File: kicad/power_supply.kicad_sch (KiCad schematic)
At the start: 47 parts, among them J2 Conn_01x02_Female, Q1 2N2905A, Q2 2N2905A, Q3 BC148, Q4 BC148, T1 Transformer_1P_2S, U11 7406, U18 LM7805_TO220, U19 LM317SP_TO220, U20 LM317L_TO92

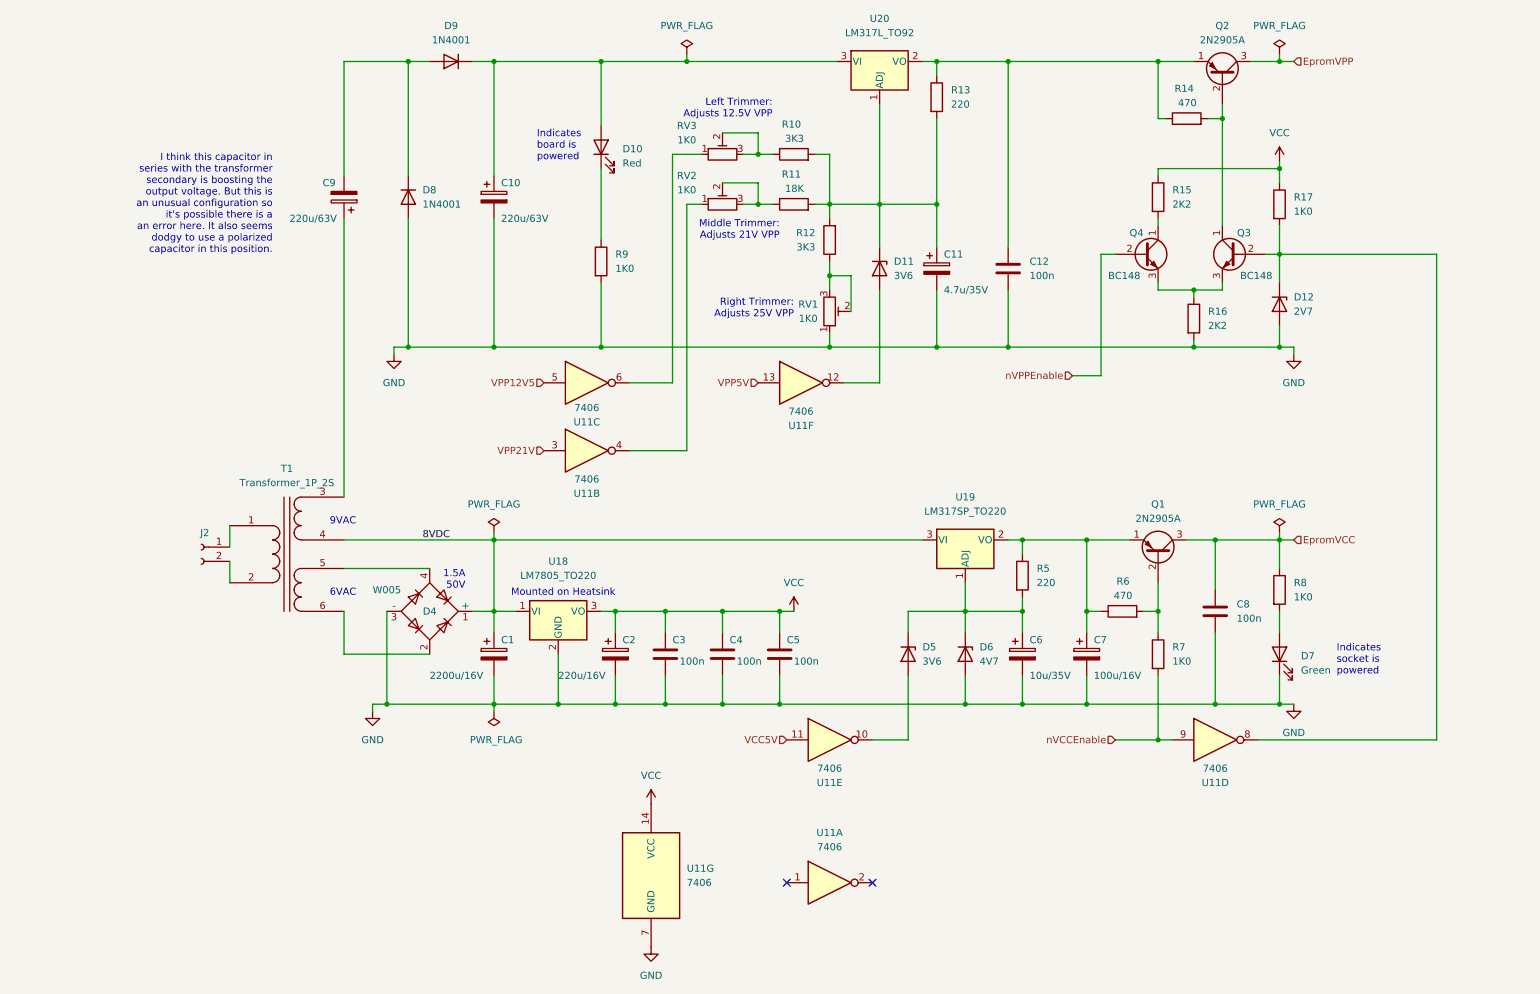
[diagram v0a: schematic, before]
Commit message: Fixed following stardot discussion of PSU, and review of issue 2 photos
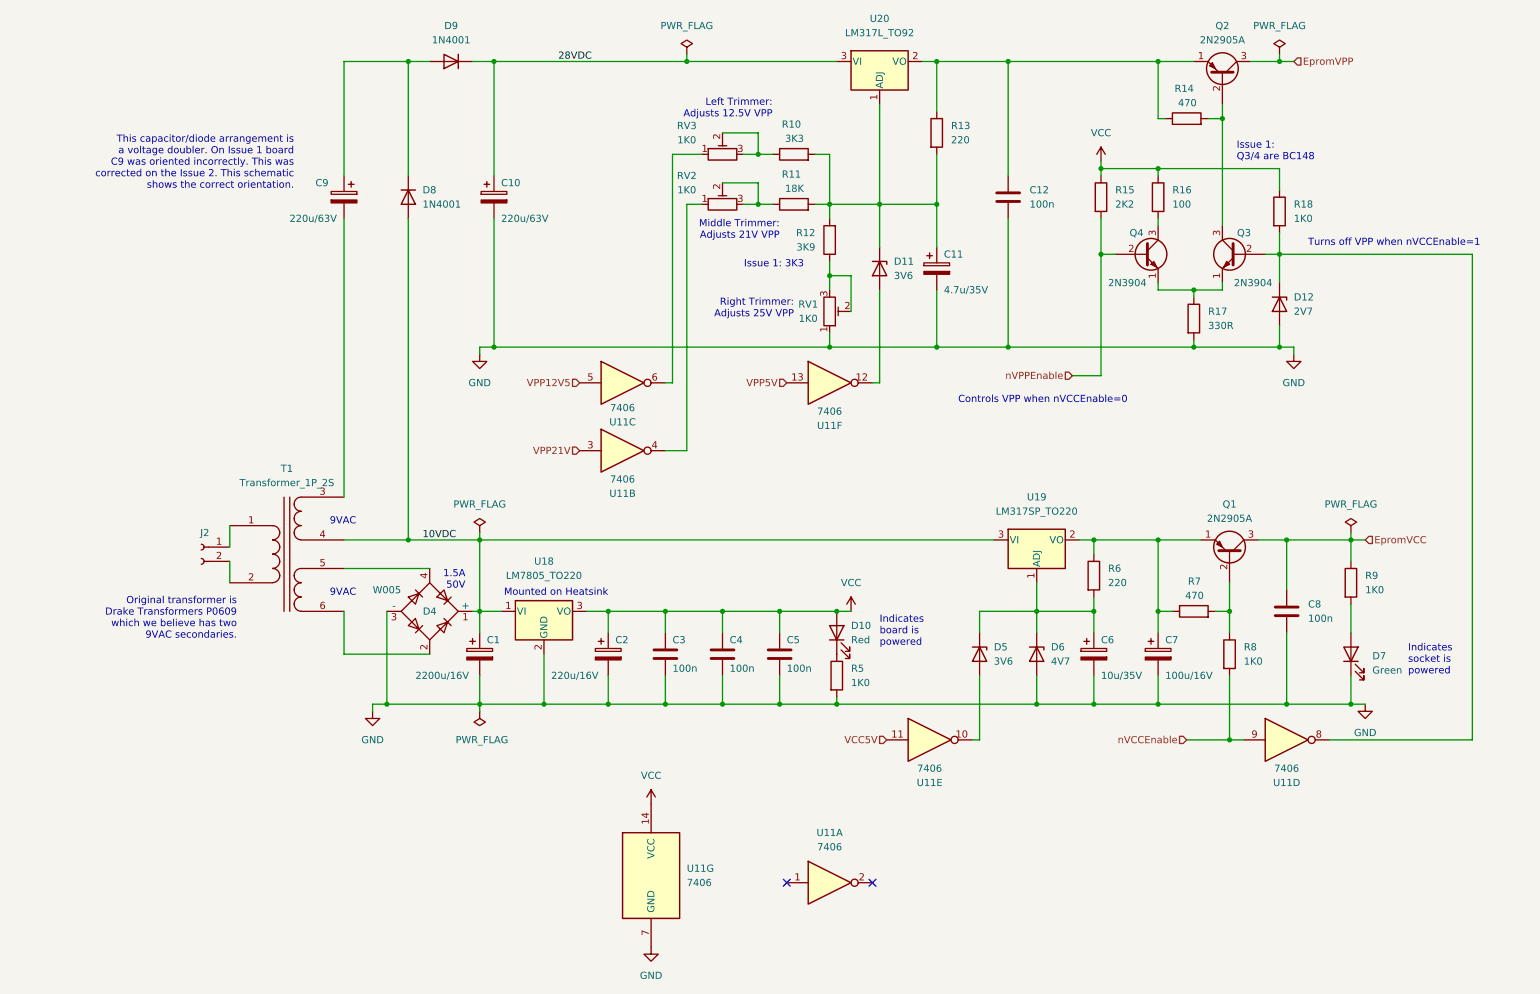
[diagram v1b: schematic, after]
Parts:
- removed Q3, Q4: BC148, Package_TO_SOT_THT:TO-92_Inline, symbol Transistor_BJT:BC548
- added Q3, Q4: 2N3904, Package_TO_SOT_THT:TO-92_Inline, symbol Transistor_BJT:2N3904
- added R16: 100, symbol Device:R
- R12: value 3K3 -> 3K9
- R17: renamed from R16; value 2K2 -> 330R
- renumbered R17 to R18, R9 to R5, R5 to R6, R6 to R7, R7 to R8, R8 to R9
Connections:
- net GND: no longer D8.2 (A)
- net VCC: now also D10.2 (A), R16.1
- net nVPPEnable: now also R15.2, Q4.2 (B)
- net at Q2.2 (B), R14.2: now also Q3.3 (C)
- net at D12.1 (K), R18.2, U11.8: now also Q3.2 (B)
- net at R17.1: now also Q3.1 (E), Q4.1 (E)
- net at T1.3 (SA): now also C9.2; no longer C9.1
- net at D8.1 (K), D9.2 (A): now also C9.1; no longer C9.2
- net 28VDC: now reaches C10.1, D9.1 (K), U20.3 (VI)
- net 28VDC: no longer D10.2 (A)
- net 8VDC renamed 10VDC
- net 10VDC: now also D8.2 (A)
- new net: Q4.3 (C), R16.2
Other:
- note added: "Controls VPP when nVCCEnable=0"
- note added: "Issue 1: 3K3"
- note added: "Issue 1: Q3/4 are BC148"
- note added: "Original transformer is Drake Transformers P0609 which we believe has two 9VAC secondaries."
- note added: "This capacitor/diode arrangement is a voltage doubler. On Issue 1 board C9 was oriented incorrectly. This was corrected on the Issue 2. This schematic shows the correct orientation."
- note added: "Turns off VPP when nVCCEnable=1"
- note removed: "6VAC"
- note removed: "I think this capacitor in series with the transformer secondary is boosting the output voltage. But this is an unusual configuration so it's possible there is a an error here. It also seems dodgy to use a polarized capacitor in this position."
- moved on the sheet: C1, C12, C2, C6, C7, C8, C9, D10, D5, D6, D7, Q1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

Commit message: KiCAD: Initial PCB placement
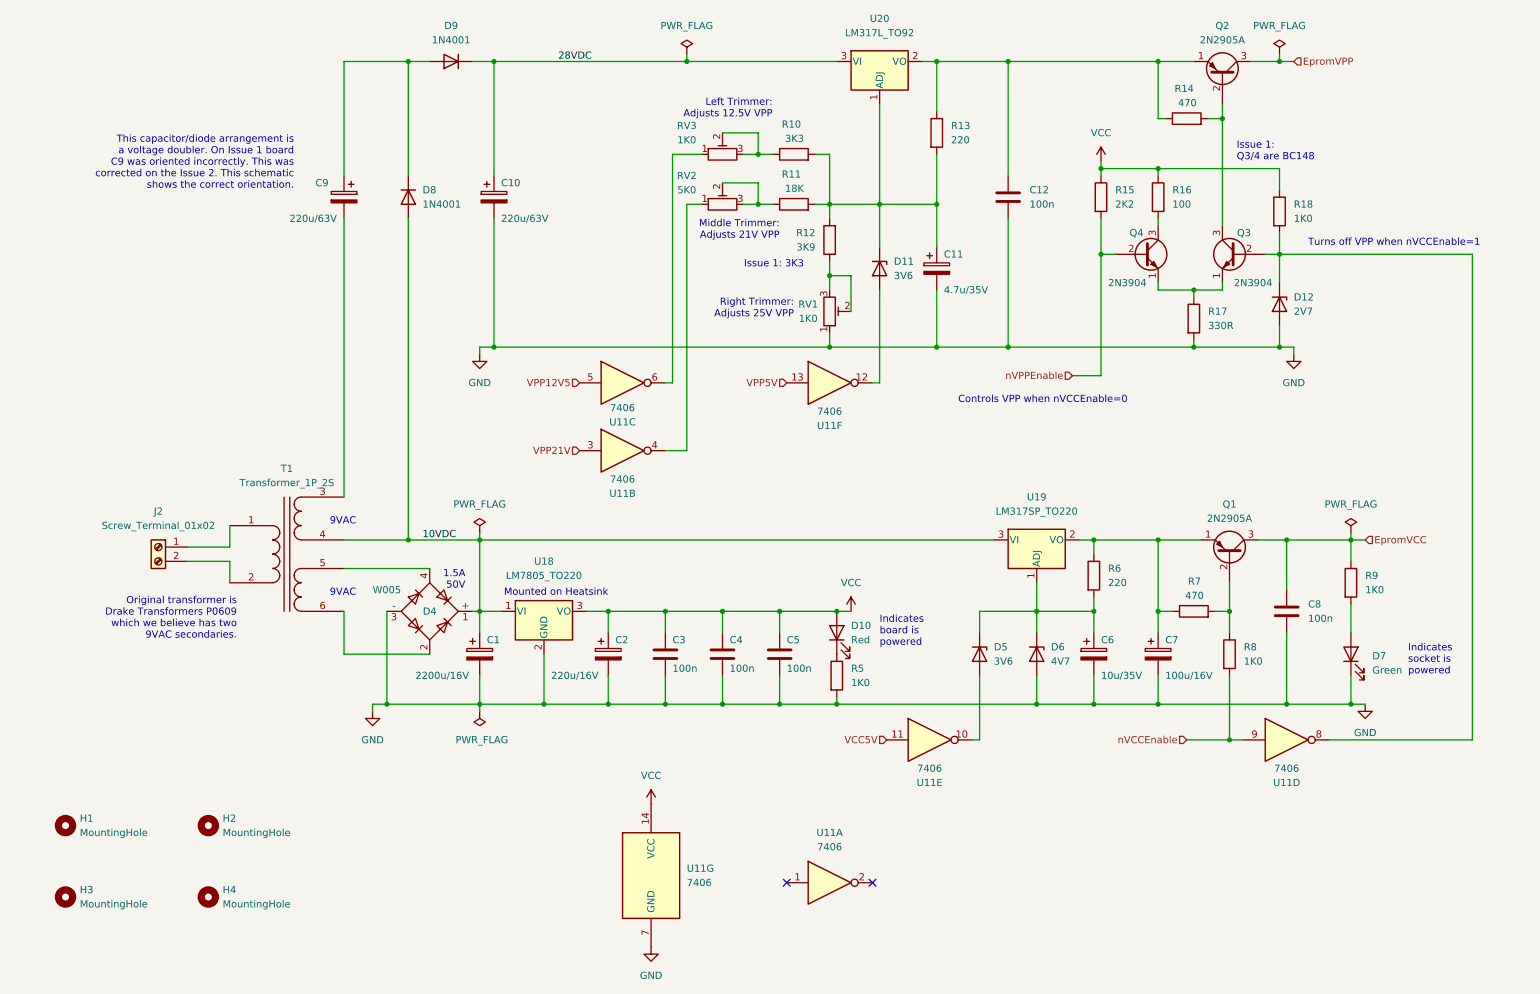
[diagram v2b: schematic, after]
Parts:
- removed J2: Conn_01x02_Female, symbol Connector:Conn_01x02_Female
- added H1, H2, H3, H4: MountingHole, MountingHole:MountingHole_2.7mm_M2.5, symbol Mechanical:MountingHole
- added J2: Screw_Terminal_01x02, TerminalBlock_Phoenix:TerminalBlock_Phoenix_MKDS-1,5-2_1x02_P5.00mm_Horizontal, symbol Connector:Screw_Terminal_01x02
- C1: footprint (none) -> Capacitor_THT:CP_Radial_D13.0mm_P5.00mm
- C10, C9: footprint (none) -> Capacitor_THT:CP_Radial_D10.0mm_P5.00mm
- C11, C6: footprint (none) -> Capacitor_THT:CP_Radial_Tantal_D4.5mm_P5.00mm
- C12, C3, C4, C5, C8: footprint (none) -> Capacitor_THT:C_Disc_D4.3mm_W1.9mm_P5.00mm
- C2: footprint (none) -> Capacitor_THT:CP_Radial_D8.0mm_P5.00mm
- C7: footprint (none) -> Capacitor_THT:CP_Radial_D6.3mm_P2.50mm
- D10, D7: footprint (none) -> LED_THT:LED_D3.0mm
- D11, D12, D5, D6: footprint (none) -> custom_footprints:D_DO-35_SOD27_P11.43mm_Horizontal
- D4: footprint Diode_THT:Diode_Bridge_Round_D9.8mm -> Diode_THT:Diode_Bridge_Round_D9.0mm
- D8, D9: footprint Diode_THT:D_DO-41_SOD81_P10.16mm_Horizontal -> custom_footprints:D_DO-41_SOD81_P11.43mm_Horizontal
- Q3, Q4: footprint Package_TO_SOT_THT:TO-92_Inline -> custom_footprints:TO-92_Wide
- R10, R11, R12, R13, R15, R16, R17, R18, R5, R6, R7, R8: footprint (none) -> custom_footprints:R_Axial_DIN0207_L6.3mm_D2.0mm_P11.43mm_Horizontal
- R14, R9: footprint (none) -> custom_footprints:R_Axial_DIN0207_L6.3mm_D2.0mm_P10.16mm_Horizontal
- RV1, RV3: footprint (none) -> Potentiometer_THT:Potentiometer_Bourns_3339P_Vertical
- RV2: value 1K0 -> 5K0; footprint (none) -> Potentiometer_THT:Potentiometer_Bourns_3339P_Vertical
- T1: footprint (none) -> custom_footprints:Transformer_vigortronix_12VA_2xSec
- U11: footprint (none) -> Package_DIP:DIP-14_W7.62mm_LongPads
- U20: footprint Package_TO_SOT_THT:TO-92_Inline -> Package_TO_SOT_THT:TO-92_Inline_Wide
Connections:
- net at T1.1 (AA): now also J2.1 (Pin_1)
- net at T1.2 (AB): now also J2.2 (Pin_2)

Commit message: KiCAD: PCB now routed
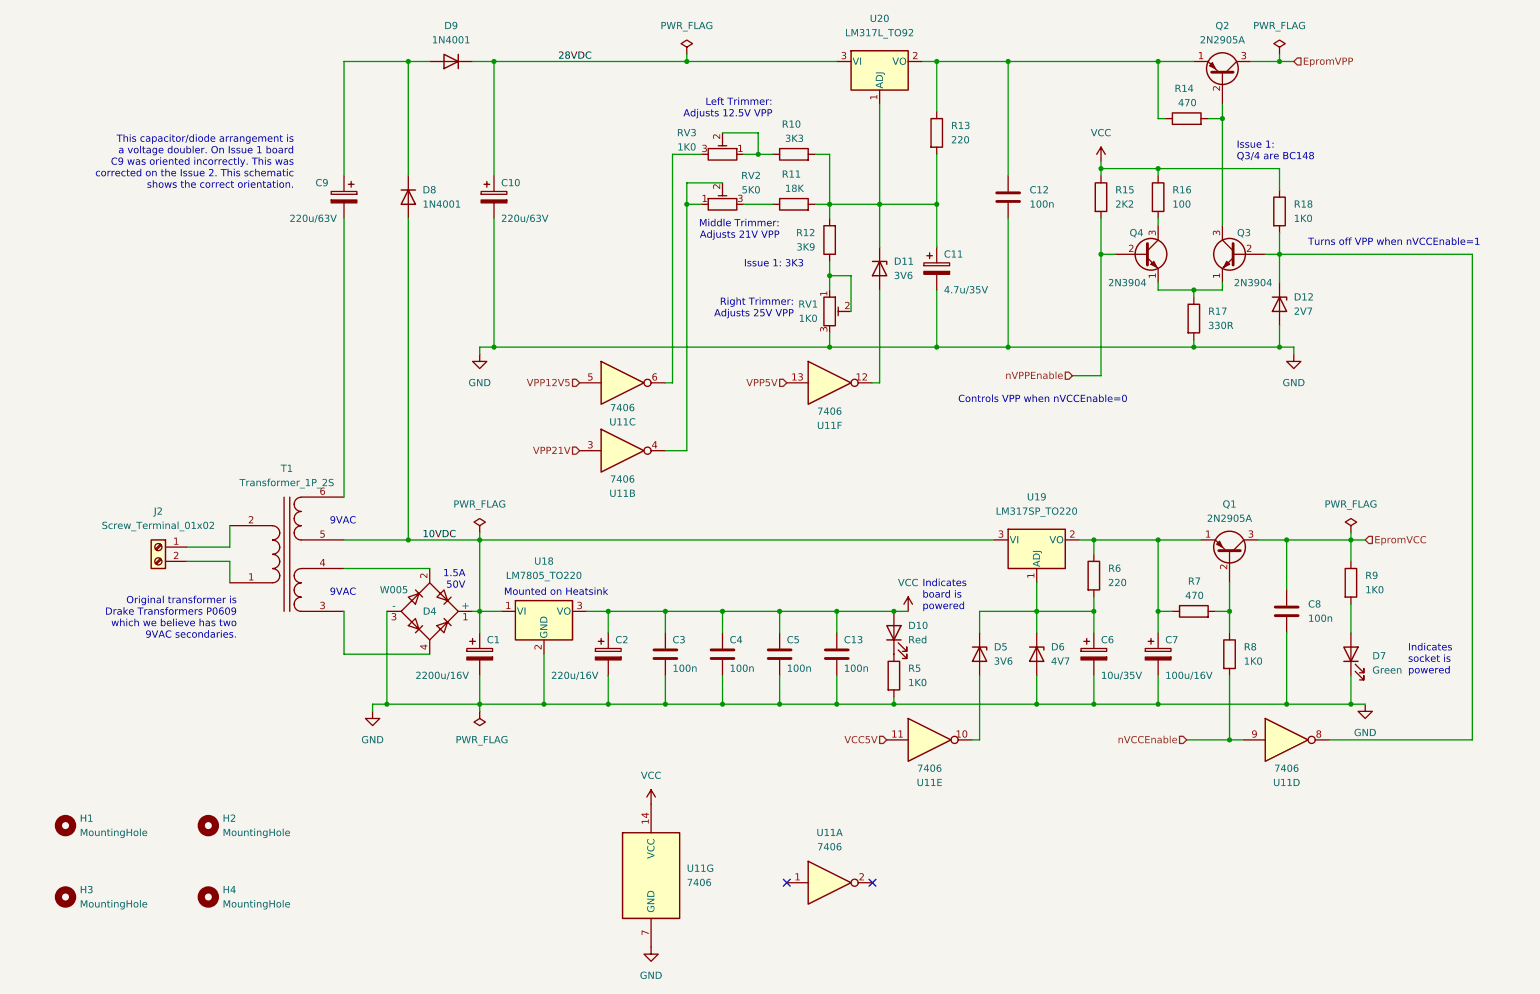
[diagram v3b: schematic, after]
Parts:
- added C13: 100n, Capacitor_THT:C_Disc_D4.3mm_W1.9mm_P5.00mm, symbol Device:C
- T1: footprint custom_footprints:Transformer_vigortronix_12VA_2xSec -> custom_footprints:Transformer_drake_p0609
- U11: footprint Package_DIP:DIP-14_W7.62mm_LongPads -> Package_DIP:DIP-14_W7.62mm
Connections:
- net 10VDC: now also T1.5 (SC); no longer T1.4 (SB)
- net GND: now also RV1.3, C13.2; no longer RV1.1
- net VCC: now also C13.1
- net at U11.6: now also RV3.3; no longer RV3.1
- net at D4.2: now also T1.4 (SB); no longer T1.6 (SD)
- net at D4.4: now also T1.3 (SA); no longer T1.5 (SC)
- net at R10.1, RV3.2: now also RV3.1; no longer RV3.3
- net at T1.1 (AA): now also J2.2 (Pin_2); no longer J2.1 (Pin_1)
- net at T1.2 (AB): now also J2.1 (Pin_1); no longer J2.2 (Pin_2)
- net at C9.2: now also T1.6 (SD); no longer T1.3 (SA)
- net at R12.1, RV1.2: now also RV1.1; no longer RV1.3
- net at R11.1, RV2.3: no longer RV2.2
- net at RV2.1, U11.4: now also RV2.2
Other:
- moved on the sheet: D10, R5, RV3

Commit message: KiCAD: Tidying errors/warnings
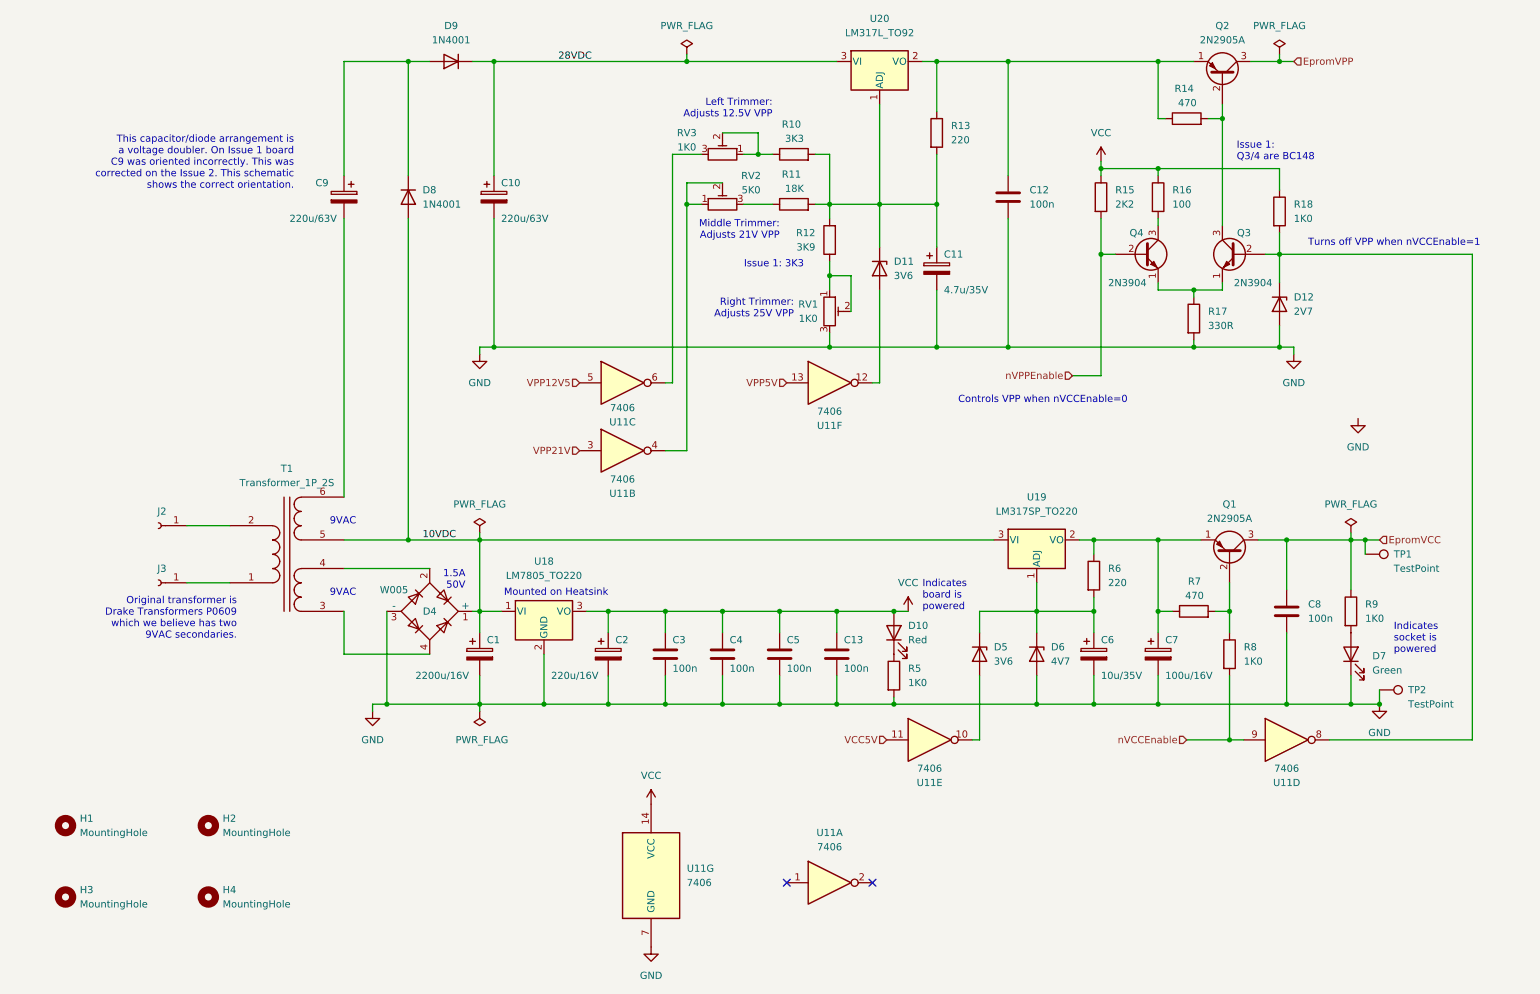
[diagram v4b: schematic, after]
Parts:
- removed J2: Screw_Terminal_01x02, TerminalBlock_Phoenix:TerminalBlock_Phoenix_MKDS-1,5-2_1x02_P5.00mm_Horizontal, symbol Connector:Screw_Terminal_01x02
- added J2, J3: Conn_01x01_Female, TestPoint:TestPoint_THTPad_D3.0mm_Drill1.5mm, symbol Connector:Conn_01x01_Female
- added TP1, TP2: TestPoint, TestPoint:TestPoint_THTPad_D1.5mm_Drill0.7mm, symbol Connector:TestPoint
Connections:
- net EpromVCC: now also TP1.1
- net GND: now also TP2.1
- net at T1.1 (AA): now also J3.1 (Pin_1)
- net at T1.2 (AB): now also J2.1 (Pin_1)
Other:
- moved on the sheet: R9
